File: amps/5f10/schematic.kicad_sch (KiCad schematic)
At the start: 42 parts, among them T1 PP OT

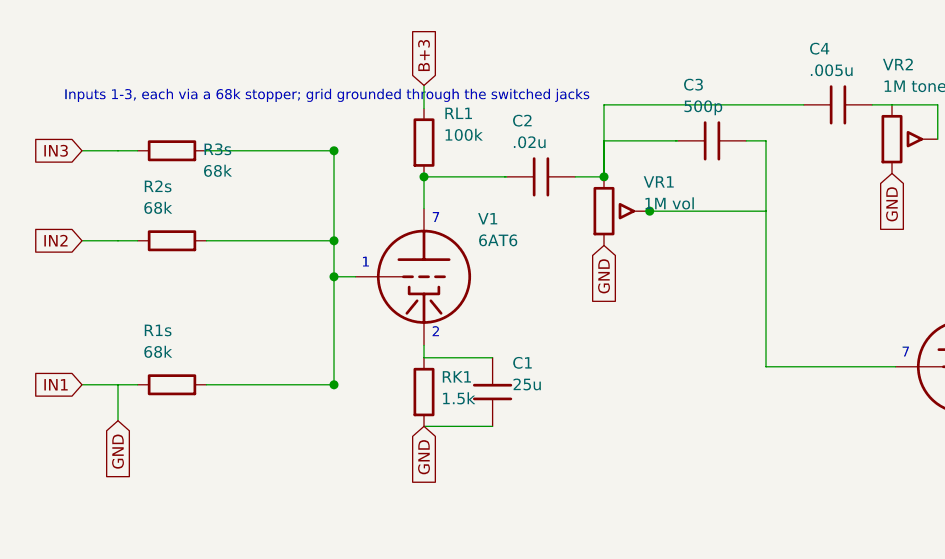
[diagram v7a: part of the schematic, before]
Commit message: Fix: tone-network gate walks 30 stacks, says what it skips; a plotted preset had never been walked
The gate that proves a schematic draws the tone network the lab plots covered
21 stacks. It now covers 30, and it names the 18 it still cannot.

The largest finding is about the gate itself. _parse_table silently dropped
any spec entry that opened with a // comment, so the 5F2-A -- a PLOTTED lab
preset -- had never been walked once: its published curve was compared against
nothing. Fixed, with an assertion that the parsed count equals the declared
count, so a spec this gate cannot read can never again be a network it
silently skips.

Nine networks newly declared and passing: DR103 (fmv ladder), the AA864's
normal and bass channels (tb ladders; the bass channel's 250k above the 50k
Treble pot is on the sheet, so the walker gained an optional trebleSeries,
proved load-bearing three ways), the 5E4-A's split network (part for part the
5F4's), and four single-knob cuts (5F10, 6G2, 6161, GA-40).

Three drawings disagree with their own cited sheets and are recorded as dated
DEFECT entries rather than declared: 6G4 both channels (no 0.05u coupler, no
0.01u slope-foot cap -- a DC path to ground through the stack), 6G5 both
channels (no slope resistor, no coupler), and the 6G6-B's normal channel (no
100k slope, no 0.1u to the 70k tap, three nodes collapsed into one) on a page
carrying a verified badge. Their repairs need parts-list entries and follow
separately.

UNCHECKED_NETWORKS is enforced, not decorative: a circuit that declares a tone
network and appears in neither the specs nor that list fails CI, as does a
stale entry naming a network now walked. 18 remain, each with its reason --
three-terminal blends the lab does not model, cascaded pots, a James board,
a differential top cut.

The lab page's absentee paragraph now sorts gated-but-unplotted circuits into
three honest buckets instead of calling five single-knob cuts a "three-knob
network". Reading the render rather than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
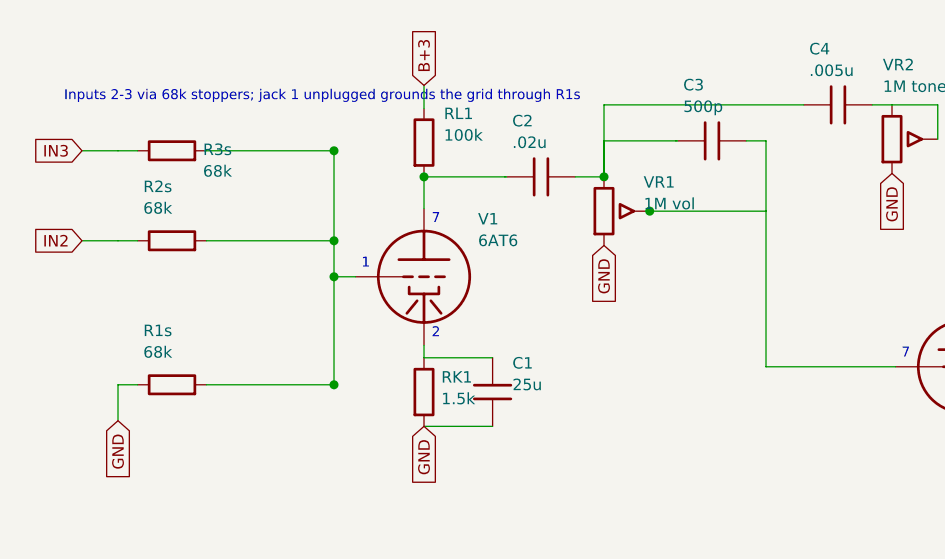
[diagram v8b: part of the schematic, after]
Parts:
- removed RB1: 6.8k, symbol cx:R
- removed RD2: 22k, symbol cx:R
- removed RKB, RNFB: 56k, symbol cx:R
- removed V3, V4: 6V6GT, symbol cx:PENTODE
- added C9: 16u, symbol cx:C
- added D1: SEL, symbol cx:DIODE_SS
- added RK2, RKA, Rs1, Rs2: 1.5k, symbol cx:R
- RB1: renamed from D1; value SEL -> 6.8k; symbol cx:DIODE_SS -> cx:R
- RD2: renamed from C9; value 16u -> 22k; symbol cx:C -> cx:R
- RKB: renamed from RKA; value 1.5k -> 56k
- RNFB: renamed from RK2; value 1.5k -> 56k
- V3: renamed from Rs1; value 1.5k -> 6V6GT; symbol cx:R -> cx:PENTODE
- V4: renamed from Rs2; value 1.5k -> 6V6GT; symbol cx:R -> cx:PENTODE
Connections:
- net -21V: now also RB1.2
- net B+2: now also V3.3 (G2), V4.3 (G2), C9.1
- net B+3: now also RD2.2
- net GND: now also RKB.2, V3.4 (K), V4.4 (K), C9.2, RK2.2; no longer RD2.2, RNFB.2
- net HT_B: now also D1.1 (A); no longer RB1.1 (A)
- net SPKR: now also RNFB.2
- net at RKB.1: now also C7.1, RGPI.2, RKA.2; no longer V2B.3 (K)
- net at RNFB.1, V2A.3 (K): now also RK2.1
- net at C7.2, RG2.1: now also Rs2.1; no longer V4.1
- net at T1.1 (PRI_A): now also V3.1 (P)
- net at V3.2 (G1): now also Rs1.2
- net at C6.2, RG1.1: now also Rs1.1; no longer V3.1
- net at T1.3 (PRI_B): now also V4.1 (P)
- net at V4.2 (G1): now also Rs2.2
- new net: RKA.1, V2B.3 (K)
- new net: D1.2 (K), RB1.1
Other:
- note added: "Inputs 2-3 via 68k stoppers; jack 1 unplugged grounds the grid through R1s"
- note removed: "Inputs 1-3, each via a 68k stopper; grid grounded through the switched jacks"
- moved on the sheet: RKB, RNFB
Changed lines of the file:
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@@
     (stroke (width 0) (type default)))
   (junction (at 45.018 34.889) (diameter 1) (color 0 0 0 0))
-  (global_label "IN1" (shape input) (at 17.018 50.889 180)
-    (effects (font (size 1.27 1.27)) (justify right)))
-  (wire (pts (xy 17.018 50.889) (xy 21.018 50.889))
-    (stroke (width 0) (type default)))
   (symbol (lib_id "cx:R") (at 27.018 50.889 90) (unit 1)
     (in_bom yes) (on_board yes)
@@
   (wire (pts (xy 45.018 38.889) (xy 45.018 50.889))
     (stroke (width 0) (type default)))
-  (text "Inputs 1-3, each via a 68k stopper; grid grounded through the switched jacks" (at 15.018 18.889 0)
+  (text "Inputs 2-3 via 68k stoppers; jack 1 unplugged grounds the grid through R1s" (at 15.018 18.889 0)
     (effects (font (size 1.1 1.1)) (justify left)))
   (symbol (lib_id "cx:TRIODE") (at 55.018 38.889 0) (unit 1)
